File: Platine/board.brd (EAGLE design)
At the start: 75 x 100 mm, 10 parts, among them T1 BC847, T2 BC847

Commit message: Update PCB
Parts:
- removed C1, C2: 100µ, resistor:C0805
- added C4, C5: 100µ, resistor:153CLV-0605
- added J1: (no value), con-jack:SPC4078
- moved R3 25.4 mm to (10.0, 30.5), turned to 270 degrees
- moved R4 17.8 mm to (28.5, 25.0), turned to 270 degrees
- moved T1 14.0 mm to (20.0, 32.5)
- moved T2 9.66 mm to (18.5, 41.5)
- moved R1 8.63 mm to (38.5, 39.5), turned to 0 degrees
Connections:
- net +5V: now also J1.3
- net GND: now also J1.1, J1.2
- net N$6: now also C4.-; no longer C1.2
- net N$7: now also C5.-; no longer C2.1
- net N$8: now also C4.+; no longer C1.1
- net N$9: now also C5.+; no longer C2.2
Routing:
- net N$13: track 4.00 -> 392.5 mm
- net N$1: track 367.8 -> 9.33 mm
- net GND: track 0.00 -> 16.7 mm
- net N$17: track 24.7 -> 11.7 mm
- net N$18: track 21.3 -> 8.91 mm
- net N$11: track 18.1 -> 6.33 mm
- net +5V: track 0.00 -> 9.78 mm
- net N$15: track 2.00 -> 7.62 mm
- net N$10: track 8.71 -> 11.7 mm
- net N$14: track 13.0 -> 10.8 mm
- net N$16: track 6.74 -> 8.41 mm

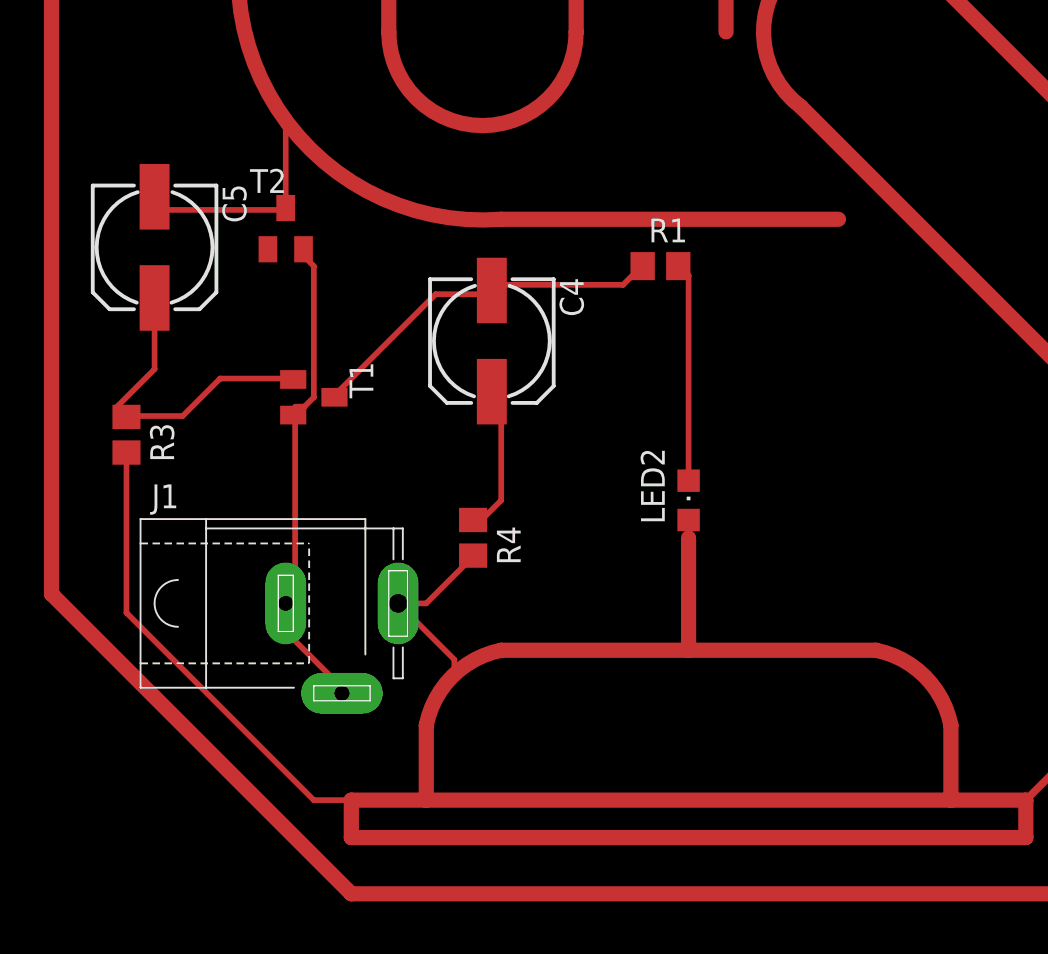
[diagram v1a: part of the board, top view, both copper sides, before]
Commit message: Update Platine: SMD Hohlstecker + Wire vergessen
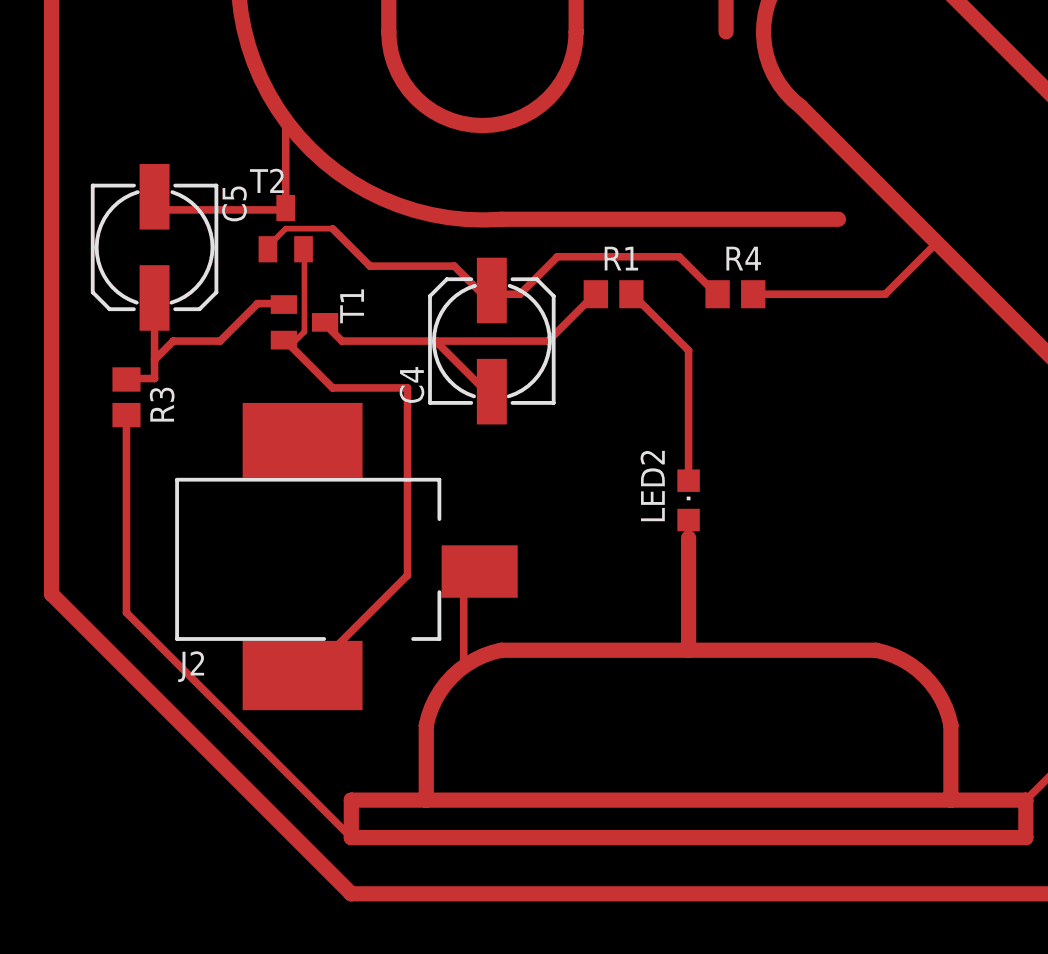
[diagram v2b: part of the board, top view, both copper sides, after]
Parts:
- removed J1: (no value), con-jack:SPC4078
- added J2: (no value), Hohlstecker-SMD:RASM7X2
- moved R4 19.1 mm to (42.5, 38.0), turned to 0 degrees
- moved T1 4.03 mm to (19.5, 36.5)
- moved R1 2.92 mm to (36.0, 38.0)
- moved R3 2.00 mm to (10.0, 32.5)
- turned C4 to 90 degrees
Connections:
- new net N$19: J2.P$1
- net +5V: now also J2.P$3; no longer J1.3
- net GND: now also J2.P$2; no longer J1.1, J1.2
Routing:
- net N$20: track 0.00 -> 394.8 mm
- net N$13: track 392.5 -> 20.2 mm
- net N$21: track 0.00 -> 23.2 mm
- net N$15: track 7.62 -> 27.5 mm
- net GND: track 16.7 -> 0.00 mm
- net +5V: track 9.78 -> 0.00 mm
- net N$18: track 8.91 -> 0.00 mm
- net N$17: track 11.7 -> 4.00 mm
- net N$1: track 9.33 -> 12.7 mm
- net N$16: track 8.41 -> 10.5 mm
- net N$11: track 6.33 -> 4.71 mm
- net N$10: track 11.7 -> 12.2 mm

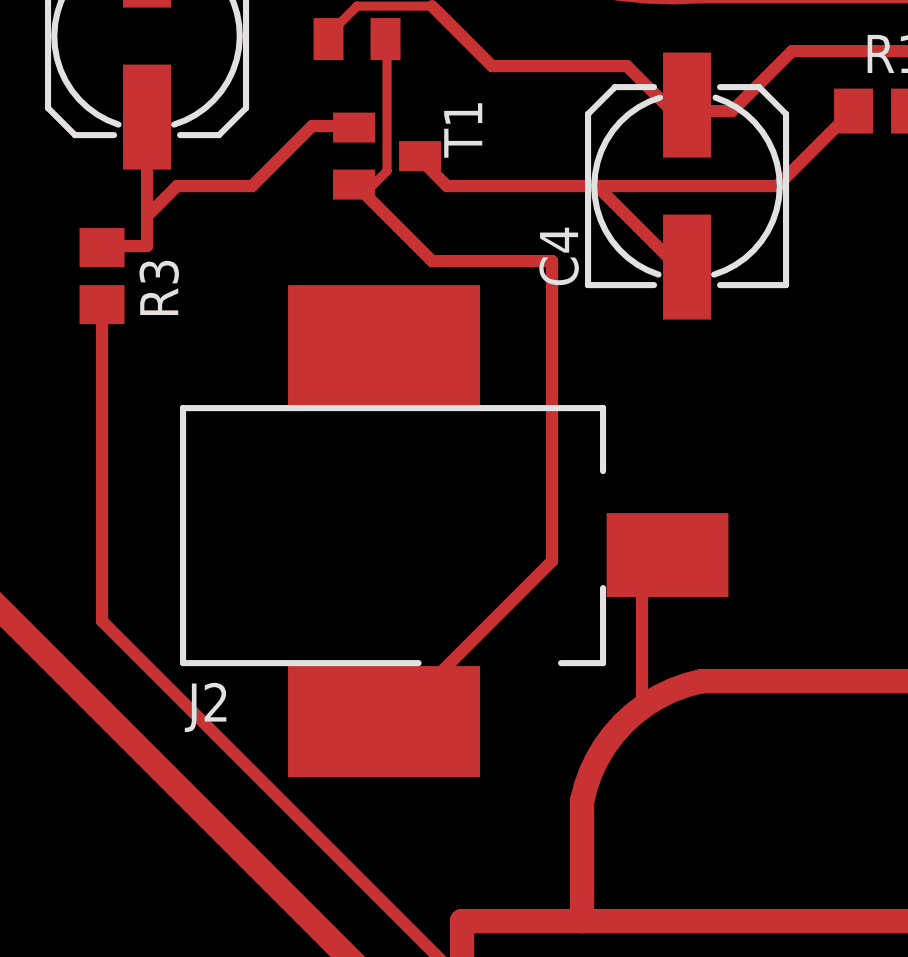
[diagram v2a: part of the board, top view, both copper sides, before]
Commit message: no text, leave the commit message out
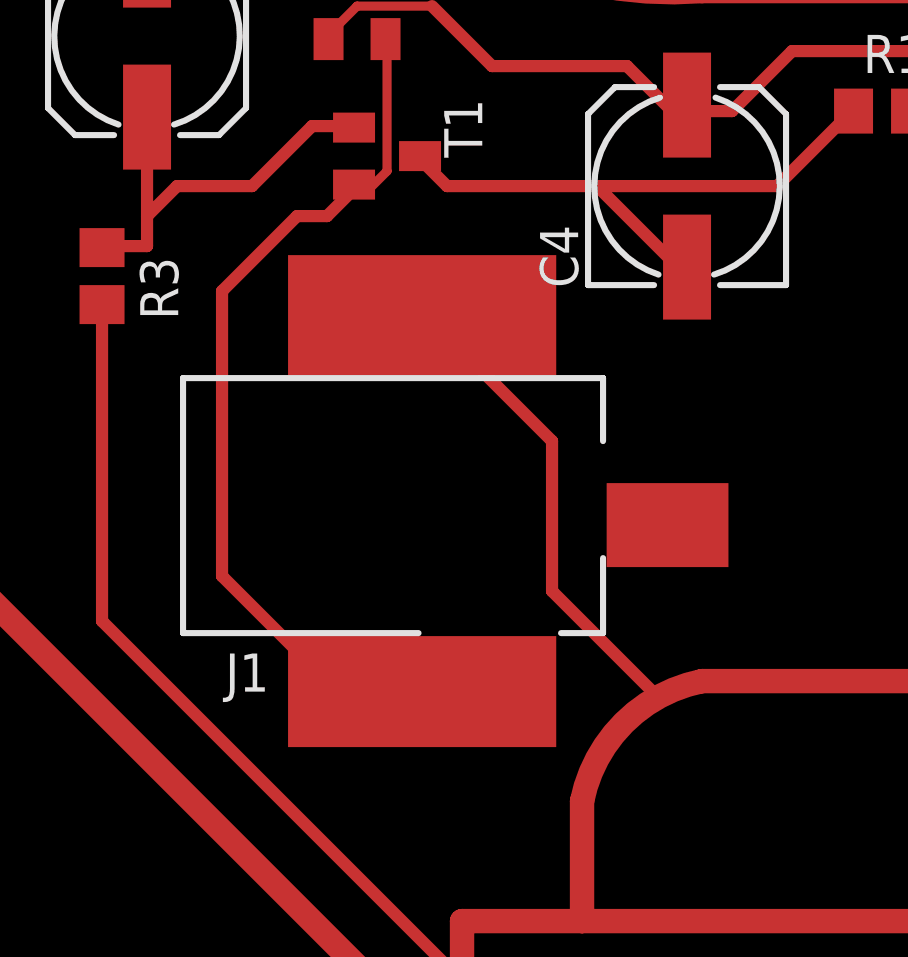
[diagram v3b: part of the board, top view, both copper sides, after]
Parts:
- removed J2: (no value), Hohlstecker-SMD:RASM7X2
- added J1: (no value), Hohlstecker-SMD:RASM7X2
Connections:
- removed net N$19: J2.P$1
- net +5V: now also J1.P$1; no longer J2.P$3
- net GND: now also J1.P$2; no longer J2.P$2
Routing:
- net N$21: track 23.2 -> 0.00 mm
- net N$17: track 4.00 -> 19.0 mm
- net N$18: track 0.00 -> 14.9 mm
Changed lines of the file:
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@@
 <attribute name="VALUE" x="6.615" y="43.925" size="1.27" layer="27" rot="R270"/>
 </element>
-<element name="J2" library="Hohlstecker-SMD" package="RASM7X2" value="" x="23" y="24" smashed="yes" rot="R270">
-<attribute name="MF" value="" x="23" y="24" size="1.778" layer="27" rot="R270" display="off"/>
-<attribute name="MPN" value="" x="23" y="24" size="1.778" layer="27" rot="R270" display="off"/>
-<attribute name="NAME" x="12.84" y="17.65" size="1.27" layer="25"/>
-<attribute name="OC_FARNELL" value="unknown" x="23" y="24" size="1.778" layer="27" rot="R270" display="off"/>
-<attribute name="OC_NEWARK" value="unknown" x="23" y="24" size="1.778" layer="27" rot="R270" display="off"/>
-<attribute name="VALUE" x="12.84" y="29.08" size="1.27" layer="27"/>
+<element name="J1" library="Hohlstecker-SMD" package="RASM7X2" value="" x="23" y="25" smashed="yes" rot="R270">
+<attribute name="MF" value="" x="23" y="25" size="1.778" layer="27" rot="R270" display="off"/>
+<attribute name="MPN" value="" x="23" y="25" size="1.778" layer="27" rot="R270" display="off"/>
+<attribute name="NAME" x="14.11" y="18.65" size="1.27" layer="25"/>
+<attribute name="OC_FARNELL" value="unknown" x="23" y="25" size="1.778" layer="27" rot="R270" display="off"/>
+<attribute name="OC_NEWARK" value="unknown" x="23" y="25" size="1.778" layer="27" rot="R270" display="off"/>
+<attribute name="VALUE" x="12.84" y="30.08" size="1.27" layer="27"/>
 </element>
 </elements>
@@
 <contactref element="R4" pad="2"/>
 <contactref element="LED1" pad="A"/>
-<contactref element="J2" pad="P$3"/>
+<contactref element="J1" pad="P$1"/>
 <wire x1="43.45" y1="38" x2="38" y2="85.95" width="0" layer="19" extent="1-1"/>
 <wire x1="40" y1="25.95" x2="43.45" y2="38" width="0" layer="19" extent="1-1"/>
-<wire x1="28.85" y1="23.2" x2="40" y2="25.95" width="0" layer="19" extent="1-1"/>
-<wire x1="10" y1="31.55" x2="28.85" y2="23.2" width="0" layer="19" extent="1-1"/>
+<wire x1="10" y1="31.55" x2="40" y2="25.95" width="0" layer="19" extent="1-1"/>
+<wire x1="20.67" y1="31.2" x2="10" y2="31.55" width="0" layer="19" extent="1-1"/>
 </signal>
 <signal name="GND">
 <contactref element="T2" pad="2"/>
 <contactref element="T1" pad="2"/>
-<contactref element="J2" pad="P$2"/>
+<contactref element="J1" pad="P$2"/>
 <wire x1="18.4" y1="35.55" x2="19.45" y2="40.4" width="0" layer="19" extent="1-1"/>
-<wire x1="19.4" y1="17.65" x2="18.4" y2="35.55" width="0" layer="19" extent="1-1"/>
+<wire x1="20.67" y1="18.65" x2="18.4" y2="35.55" width="0" layer="19" extent="1-1"/>
 </signal>
 <signal name="N$6">
@@
 <wire x1="10" y1="21" x2="22" y2="9" width="0.4064" layer="1"/>
 </signal>
-<signal name="N$19">
-<contactref element="J2" pad="P$1"/>
-</signal>
 <signal name="N$1">
 <wire x1="10" y1="33.5" x2="11.5" y2="33.5" width="0.4064" layer="1"/>
@@
 <wire x1="19" y1="35.5" x2="19.5" y2="36" width="0.3048" layer="1"/>
 <wire x1="19.5" y1="36" x2="19.5" y2="40" width="0.3048" layer="1"/>
-</signal>
-<signal name="N$17">
-<wire x1="28" y1="22" x2="28" y2="18" width="0.4064" layer="1"/>
-</signal>
-<signal name="N$21">
-<wire x1="18.5" y1="35.5" x2="21" y2="33" width="0.4064" layer="1"/>
-<wire x1="21" y1="33" x2="25" y2="33" width="0.4064" layer="1"/>
-<wire x1="25" y1="33" x2="25" y2="23" width="0.4064" layer="1"/>
-<wire x1="25" y1="23" x2="21" y2="19" width="0.4064" layer="1"/>
 </signal>
 <signal name="N$13">
@@
 <wire x1="50.5" y1="38" x2="53" y2="40.5" width="0.4064" layer="1"/>
 </signal>
+<signal name="N$17">
+<wire x1="18.5" y1="35.5" x2="17.5" y2="34.5" width="0.4064" layer="1"/>
+<wire x1="17.5" y1="34.5" x2="16.5" y2="34.5" width="0.4064" layer="1"/>
+<wire x1="16.5" y1="34.5" x2="14" y2="32" width="0.4064" layer="1"/>
+<wire x1="14" y1="32" x2="14" y2="22.5" width="0.4064" layer="1"/>
+<wire x1="14" y1="22.5" x2="16.5" y2="20" width="0.4064" layer="1"/>
+</signal>
+<signal name="N$18">
+<wire x1="21.5" y1="30.5" x2="25" y2="27" width="0.4064" layer="1"/>
+<wire x1="25" y1="27" x2="25" y2="22" width="0.4064" layer="1"/>
+<wire x1="25" y1="22" x2="28.5" y2="18.5" width="0.4064" layer="1"/>
+</signal>
 </signals>
